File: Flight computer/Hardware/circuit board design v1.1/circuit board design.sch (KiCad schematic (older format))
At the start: 0 parts

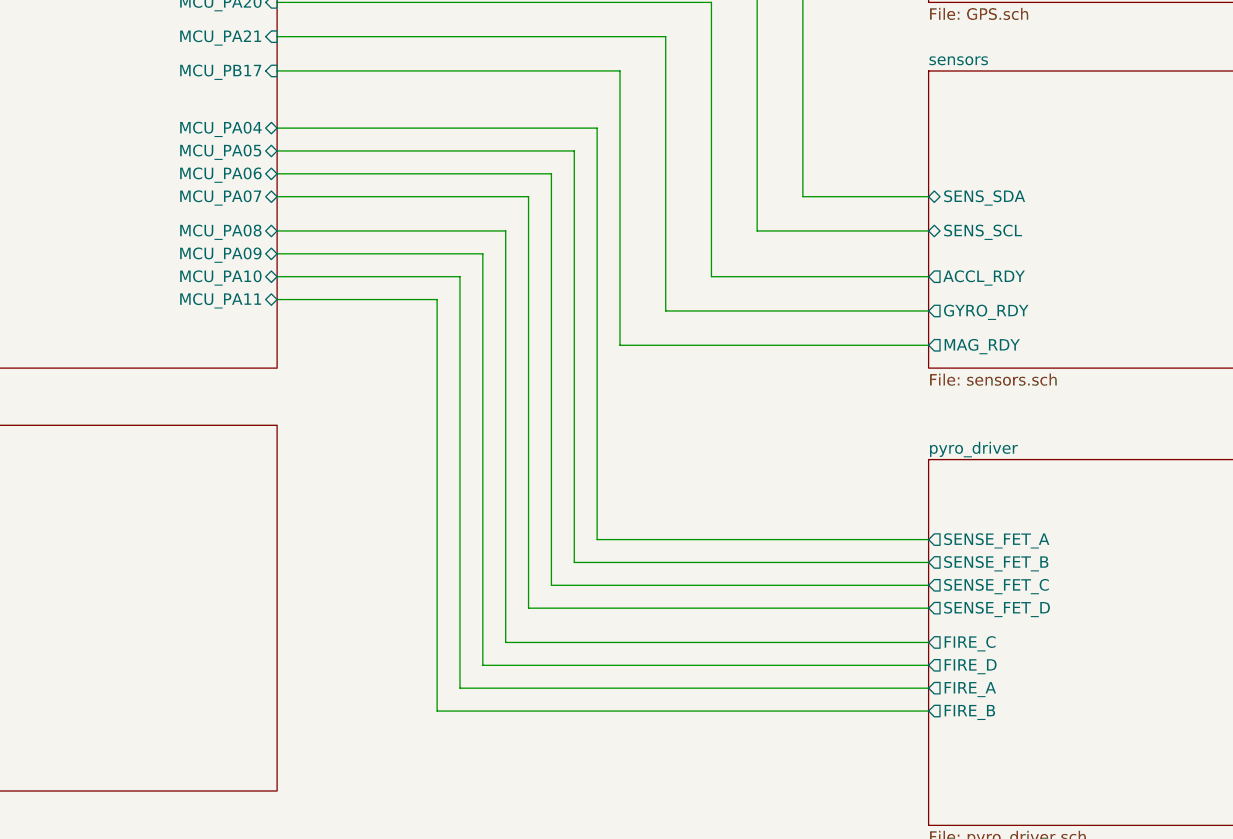
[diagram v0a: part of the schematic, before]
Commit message: put in new acclerometers and 9dof sensor. Changed supplier from mouser to farnell and RS
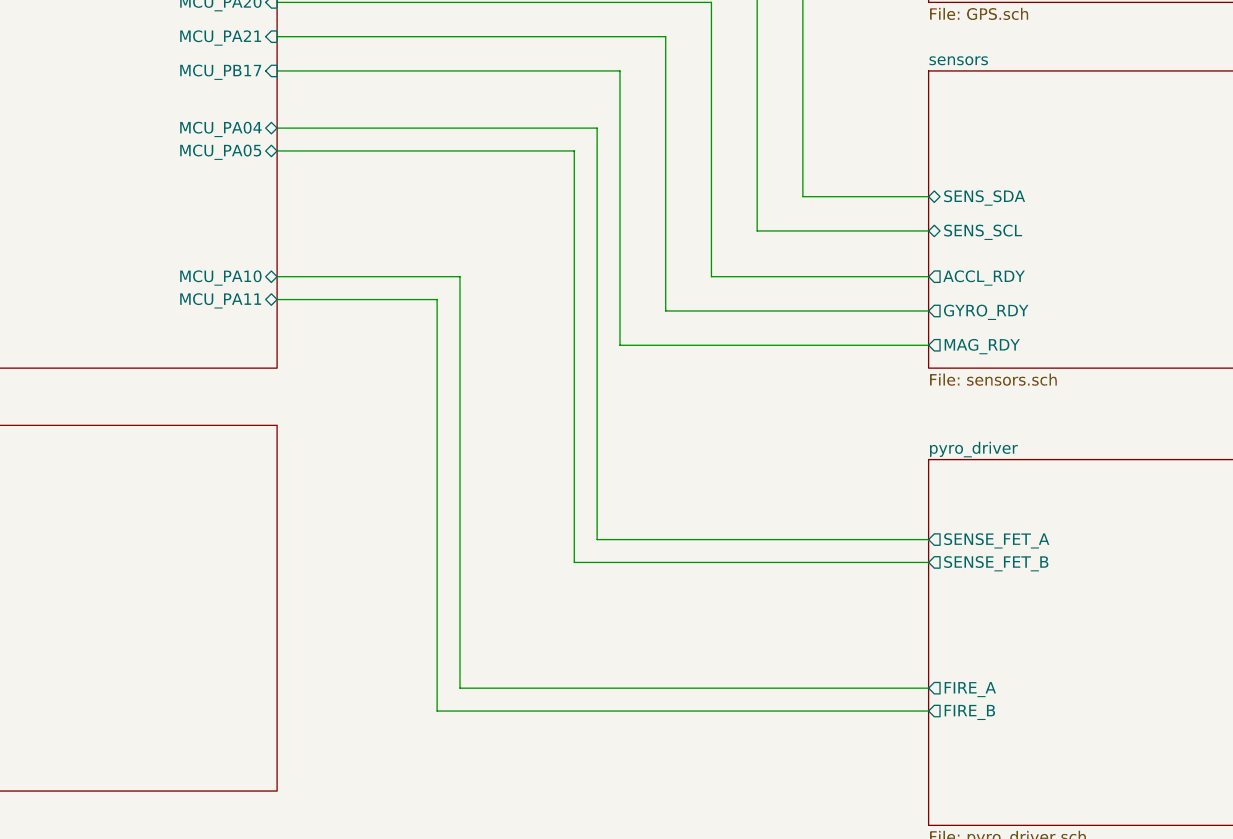
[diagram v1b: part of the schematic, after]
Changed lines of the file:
@@
 	6350 5150 6350 3350
-Wire Wire Line
-	6250 3450 6250 5250
-Wire Wire Line
-	7900 5350 6150 5350
-Wire Wire Line
-	6250 5250 7900 5250
 Wire Wire Line
 	2700 5850 1450 5850
@@
 Wire Wire Line
 	5050 3900 5850 3900
-Wire Wire Line
-	5950 3800 5050 3800
-Wire Wire Line
-	5050 3700 6050 3700
 Wire Wire Line
 	6350 3350 5050 3350
@@
 	700  6900 2700 6900
 Wire Wire Line
-	5050 3450 6250 3450
-Wire Wire Line
-	5950 5600 5950 3800
-Wire Wire Line
 	5750 5800 5750 4000
 Wire Wire Line
@@
 	5850 5700 7900 5700
 Wire Wire Line
-	7900 5600 5950 5600
-Wire Wire Line
-	6050 5500 7900 5500
-Wire Wire Line
 	5850 3900 5850 5700
-Wire Wire Line
-	6050 3700 6050 5500
-Wire Wire Line
-	6150 5350 6150 3550
-Wire Wire Line
-	5050 3550 6150 3550
 Wire Wire Line
 	6550 4200 7900 4200
@@
 	5050 2350 7900 2350
 $Sheet
+S 7900 4700 2350 1600
+U 5D6468D5
+F0 "pyro_driver" 50
+F1 "pyro_driver.sch" 50
+F2 "SENSE_FET_A" O L 7900 5050 50
+F3 "FIRE_A" O L 7900 5700 50
+F4 "SENSE_FET_B" O L 7900 5150 50
+F5 "FIRE_B" O L 7900 5800 50
+$EndSheet
+$Sheet
 S 2700 1100 2350 3200
 U 5D5B15F7
@@
 F8 "MCU_PA02" I R 5050 2200 50
 F9 "MCU_PA05" B R 5050 3350 50
-F10 "MCU_PA06" B R 5050 3450 50
-F11 "MCU_PA07" B R 5050 3550 50
-F12 "MCU_PA20" I R 5050 2700 50
-F13 "MCU_PA21" I R 5050 2850 50
-F14 "USB_DP" I L 2700 1500 50
-F15 "USB_DM" I L 2700 1400 50
-F16 "GPS_TXD0" O R 5050 1450 50
-F17 "GPS_RXD0" I R 5050 1300 50
-F18 "MCU_PA08" B R 5050 3700 50
-F19 "MCU_PA09" B R 5050 3800 50
-F20 "MCU_PA10" B R 5050 3900 50
-F21 "MCU_PA11" B R 5050 4000 50
-F22 "MCU_PA04" B R 5050 3250 50
-F23 "MCU_PA12" B L 2700 2250 50
-F24 "MCU_PA13" B L 2700 2400 50
-F25 "MCU_PB11" I L 2700 2700 50
-F26 "MCU_PB17" I R 5050 3000 50
-F27 "MCU_PB08" I L 2700 1600 50
-F28 "MCU_PA01" I R 5050 2050 50
-F29 "MCU_PA03" I R 5050 2350 50
-F30 "MCU_PB10" I L 2700 2550 50
-$EndSheet
-$Sheet
-S 7900 4700 2350 1600
-U 5D6468D5
-F0 "pyro_driver" 50
-F1 "pyro_driver.sch" 50
-F2 "SENSE_FET_A" O L 7900 5050 50
-F3 "FIRE_A" O L 7900 5700 50
-F4 "SENSE_FET_B" O L 7900 5150 50
-F5 "FIRE_B" O L 7900 5800 50
-F6 "SENSE_FET_C" O L 7900 5250 50
-F7 "FIRE_C" O L 7900 5500 50
-F8 "SENSE_FET_D" O L 7900 5350 50
-F9 "FIRE_D" O L 7900 5600 50
+F10 "MCU_PA20" I R 5050 2700 50
+F11 "MCU_PA21" I R 5050 2850 50
+F12 "USB_DP" I L 2700 1500 50
+F13 "USB_DM" I L 2700 1400 50
+F14 "GPS_TXD0" O R 5050 1450 50
+F15 "GPS_RXD0" I R 5050 1300 50
+F16 "MCU_PA10" B R 5050 3900 50
+F17 "MCU_PA11" B R 5050 4000 50
+F18 "MCU_PA04" B R 5050 3250 50
+F19 "MCU_PA12" B L 2700 2250 50
+F20 "MCU_PA13" B L 2700 2400 50
+F21 "MCU_PB11" I L 2700 2700 50
+F22 "MCU_PB17" I R 5050 3000 50
+F23 "MCU_PB08" I L 2700 1600 50
+F24 "MCU_PA01" I R 5050 2050 50
+F25 "MCU_PA03" I R 5050 2350 50
+F26 "MCU_PB10" I L 2700 2550 50
 $EndSheet
 $EndSCHEMATC

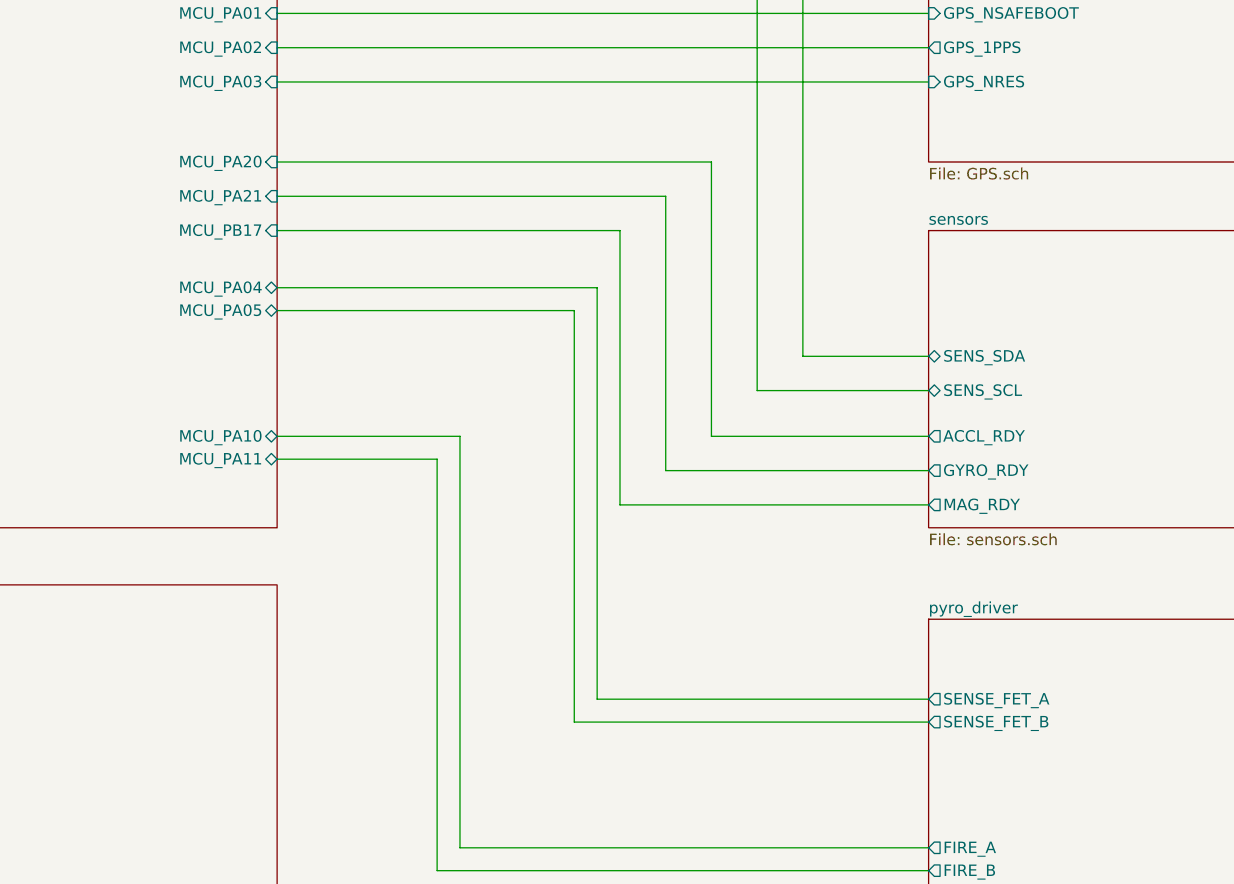
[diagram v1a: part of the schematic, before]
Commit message: wired up the news sensors
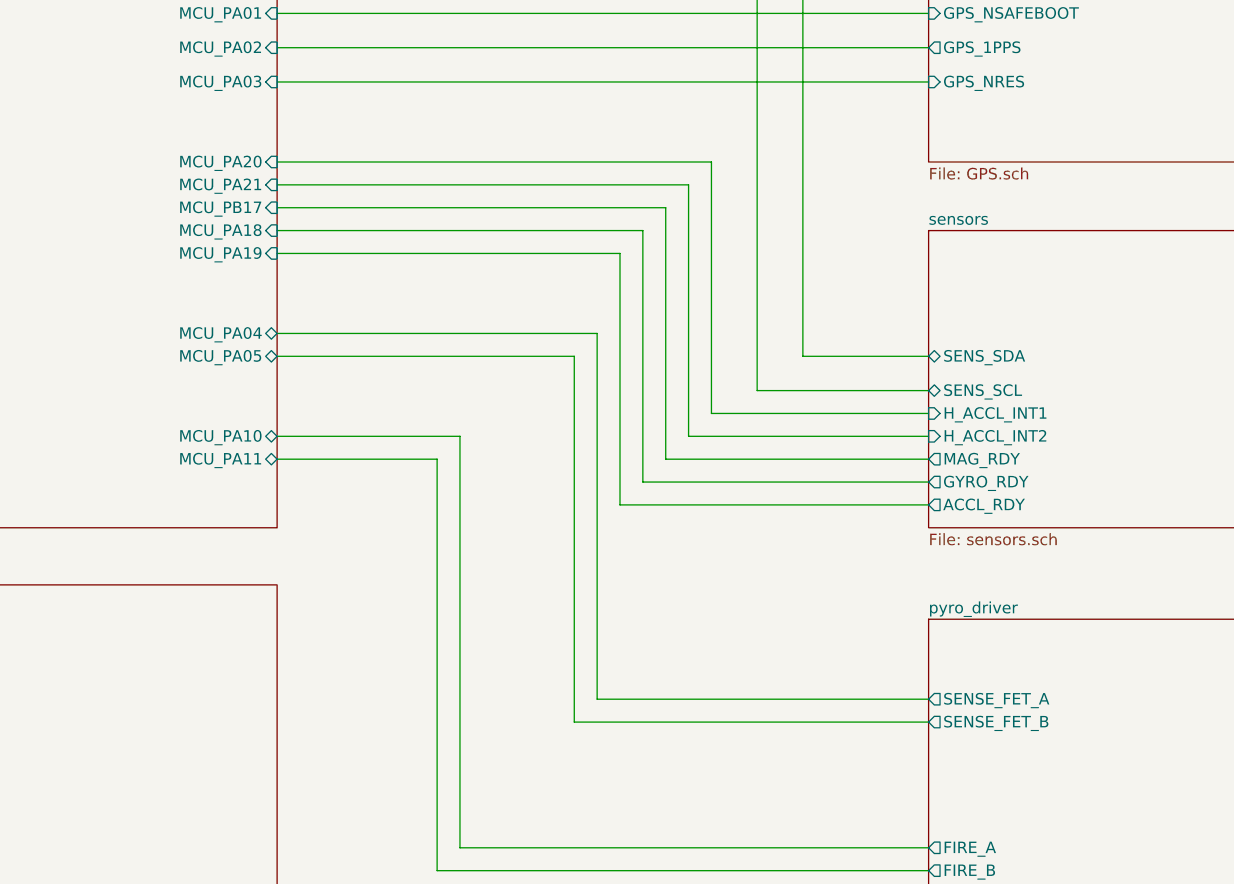
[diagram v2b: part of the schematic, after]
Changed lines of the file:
@@
 F2 "SENS_SDA" B L 7900 3550 50
 F3 "SENS_SCL" B L 7900 3700 50
-F4 "MAG_RDY" O L 7900 4200 50
-F5 "ACCL_RDY" O L 7900 3900 50
-F6 "GYRO_RDY" O L 7900 4050 50
+F4 "MAG_RDY" O L 7900 4000 50
+F5 "ACCL_RDY" O L 7900 4200 50
+F6 "GYRO_RDY" O L 7900 4100 50
+F7 "H_ACCL_INT1" I L 7900 3800 50
+F8 "H_ACCL_INT2" I L 7900 3900 50
 $EndSheet
 $Sheet
@@
 $EndSheet
 Wire Wire Line
-	6450 3250 6450 5050
+	6450 3450 6450 5050
 Wire Wire Line
 	6450 5050 7900 5050
@@
 	7900 5150 6350 5150
 Wire Wire Line
-	6350 5150 6350 3350
+	6350 5150 6350 3550
 Wire Wire Line
 	2700 5850 1450 5850
@@
 	5050 3900 5850 3900
 Wire Wire Line
-	6350 3350 5050 3350
-Wire Wire Line
-	5050 3250 6450 3250
+	6350 3550 5050 3550
+Wire Wire Line
+	5050 3450 6450 3450
 Wire Wire Line
 	5050 1450 7900 1450
@@
 	5850 3900 5850 5700
 Wire Wire Line
-	6550 4200 7900 4200
-Wire Wire Line
-	6950 3900 6950 2700
-Wire Wire Line
-	6750 4050 6750 2850
-Wire Wire Line
-	6550 3000 6550 4200
-Wire Wire Line
-	7900 4050 6750 4050
-Wire Wire Line
-	7900 3900 6950 3900
+	6750 4000 7900 4000
+Wire Wire Line
+	6750 2900 6750 4000
+Wire Wire Line
+	7900 3800 6950 3800
 Wire Wire Line
 	6950 2700 5050 2700
 Wire Wire Line
-	6750 2850 5050 2850
-Wire Wire Line
-	5050 3000 6550 3000
+	6850 2800 5050 2800
+Wire Wire Line
+	5050 2900 6750 2900
 Wire Wire Line
 	5050 1300 7900 1300
@@
 F5 "FIRE_B" O L 7900 5800 50
 $EndSheet
+Wire Wire Line
+	6950 3800 6950 2700
+Wire Wire Line
+	6850 3900 6850 2800
+Wire Wire Line
+	6850 3900 7900 3900
 $Sheet
 S 2700 1100 2350 3200
@@
 F7 "MCU_SCL3" B R 5050 1900 50
 F8 "MCU_PA02" I R 5050 2200 50
-F9 "MCU_PA05" B R 5050 3350 50
+F9 "MCU_PA05" B R 5050 3550 50
 F10 "MCU_PA20" I R 5050 2700 50
-F11 "MCU_PA21" I R 5050 2850 50
+F11 "MCU_PA21" I R 5050 2800 50
 F12 "USB_DP" I L 2700 1500 50
 F13 "USB_DM" I L 2700 1400 50
@@
 F16 "MCU_PA10" B R 5050 3900 50
 F17 "MCU_PA11" B R 5050 4000 50
-F18 "MCU_PA04" B R 5050 3250 50
+F18 "MCU_PA04" B R 5050 3450 50
 F19 "MCU_PA12" B L 2700 2250 50
 F20 "MCU_PA13" B L 2700 2400 50
 F21 "MCU_PB11" I L 2700 2700 50
-F22 "MCU_PB17" I R 5050 3000 50
+F22 "MCU_PB17" I R 5050 2900 50
 F23 "MCU_PB08" I L 2700 1600 50
 F24 "MCU_PA01" I R 5050 2050 50
 F25 "MCU_PA03" I R 5050 2350 50
 F26 "MCU_PB10" I L 2700 2550 50
-$EndSheet
+F27 "MCU_PA18" I R 5050 3000 50
+F28 "MCU_PA19" I R 5050 3100 50
+$EndSheet
+Wire Wire Line
+	5050 3000 6650 3000
+Wire Wire Line
+	6650 3000 6650 4100
+Wire Wire Line
+	6650 4100 7900 4100
+Wire Wire Line
+	7900 4200 6550 4200
+Wire Wire Line
+	6550 4200 6550 3100
+Wire Wire Line
+	6550 3100 5050 3100
 $EndSCHEMATC
